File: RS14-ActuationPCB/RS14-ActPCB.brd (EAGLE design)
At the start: 105.1 x 80 mm, 34 parts, among them IC1 L293D, IC2 L293D, P12V 22-23-2021, T1 2N3904, T2 2N3904, T3 2N3904, T4 2N3904

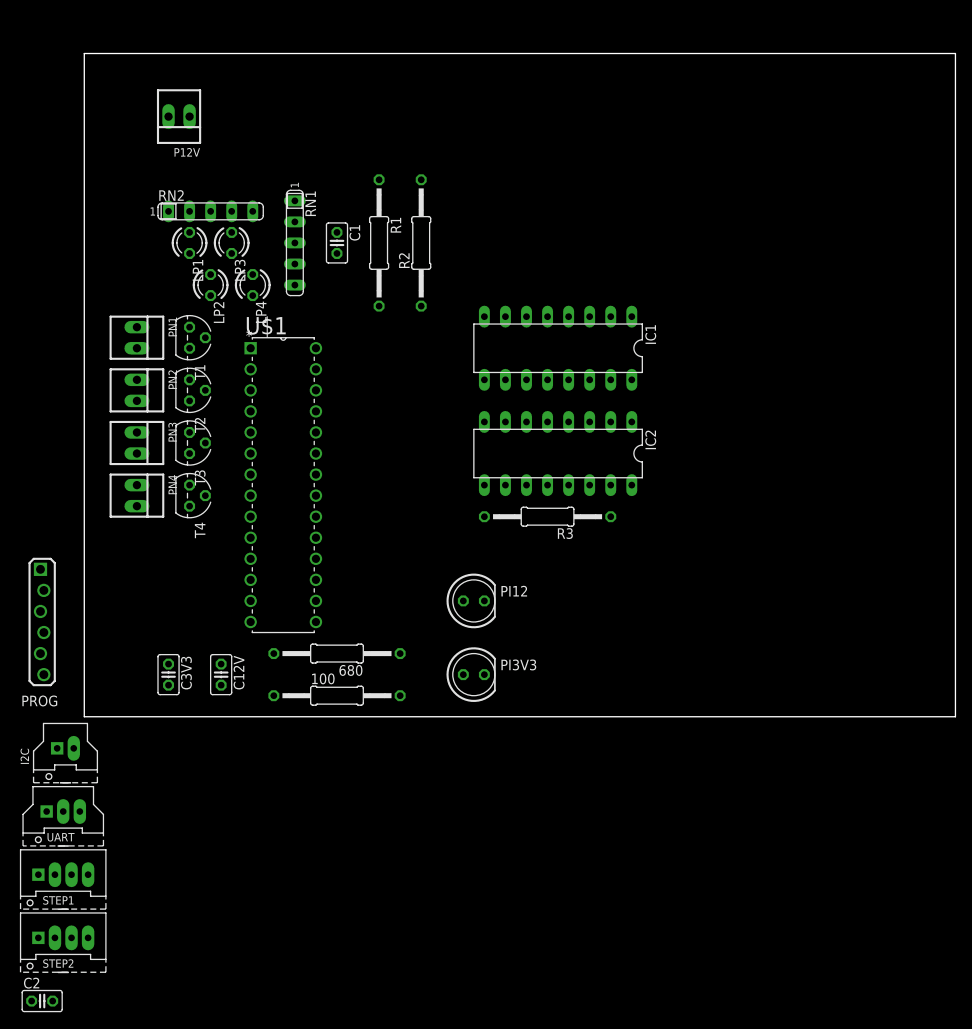
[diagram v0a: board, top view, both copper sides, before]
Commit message: Updated Actuation PCB
This is the first draft layout.

It only has two of the four desired screw holes, but this is mainly due
to my refusal to make the board bigger in my tired stubbornness. There
is also no labeling on the board (other than small built in markers) as
of yet. So this will need to be added as well.
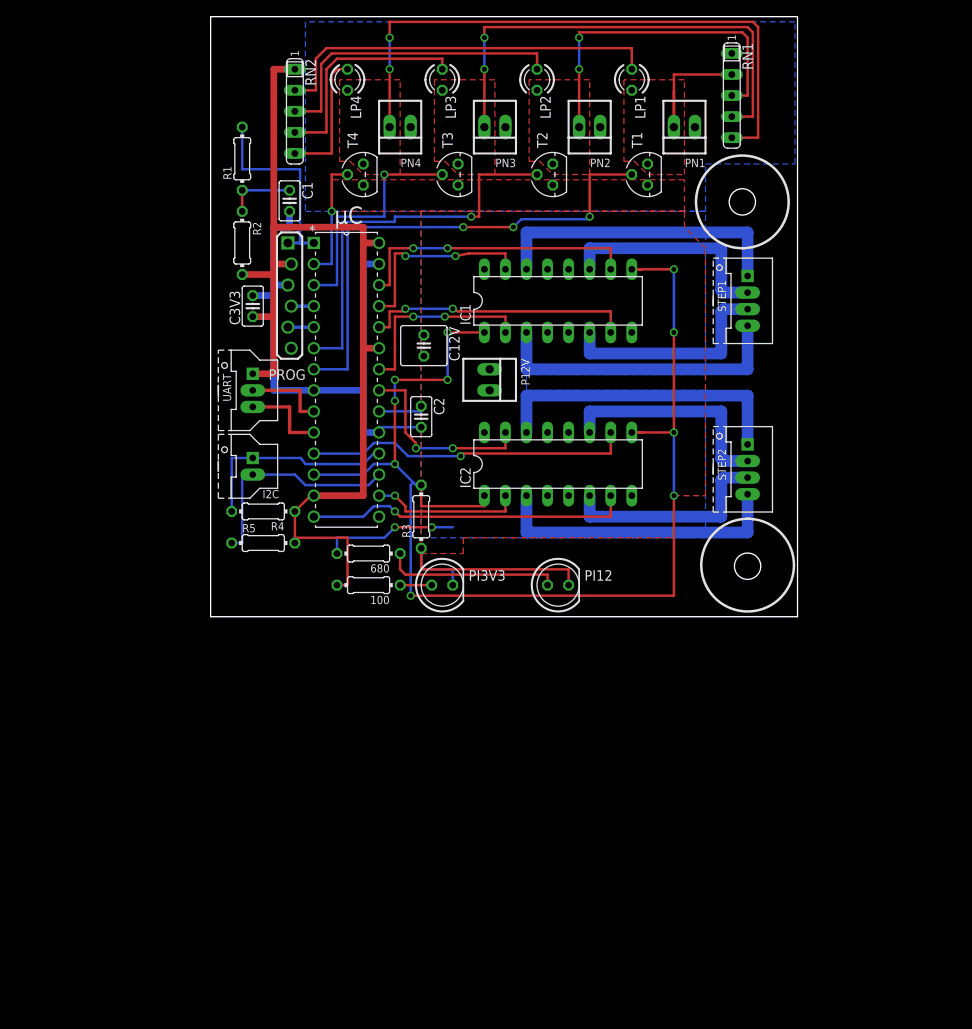
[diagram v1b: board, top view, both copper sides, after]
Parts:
- removed U$1: PIC32MX250F128B-I/SP, Microchip_By_element14_Batch_1:DIP254P762X508-28
- added R4, R5: 2K2, rcl:0204/7
- added µC: PIC32MX250F128B-I/SP, Microchip_By_element14_Batch_1:DIP254P762X508-28
- 100, 680, R1, R2, R3: device rcl:0207/15 -> rcl:0204/7
- C12V: device rcl:C025-025X050 -> rcl:C025-060X050
- moved STEP1 107.7 mm to (74.9, 50.2), turned to 270 degrees
- moved STEP2 100.0 mm to (74.9, 29.8), turned to 270 degrees
- moved C2 84.0 mm to (35.6, 36.2), turned to 270 degrees
- moved PN1 70.8 mm to (67.3, 71.1), turned to 180 degrees
- moved PN2 63.2 mm to (55.9, 71.1), turned to 180 degrees
- moved T1 58.6 mm to (62.9, 65.4), turned to 90 degrees
- moved PN3 57.6 mm to (44.5, 71.1), turned to 180 degrees
- moved LP1 56.9 mm to (61.0, 76.8)
- moved UART 55.7 mm to (15.2, 39.4), turned to 270 degrees
- moved RN1 55.6 mm to (73.0, 74.9)
- moved PN4 54.6 mm to (33.0, 71.1), turned to 180 degrees
- moved T2 51.0 mm to (51.4, 65.4), turned to 90 degrees
- moved PROG 49.4 mm to (19.7, 50.8)
- moved P12V 49.1 mm to (43.8, 40.6), turned to 270 degrees
- moved C12V 46.6 mm to (35.9, 44.8)
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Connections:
- removed net N$1: C2.2
- net 3V3: now also R4.2, R5.2, µC.13, µC.23, µC.28; no longer U$1.13, U$1.23, U$1.28
- net GND: now also C2.2, µC.19, µC.27, µC.8; no longer U$1.19, U$1.27, U$1.8
- net MCLR: now also µC.1; no longer U$1.1
- net N$2: now also µC.20; no longer U$1.20
- net PC1: now also µC.7; no longer U$1.2
- net PC2: now also µC.6; no longer U$1.3
- net PC3: now also µC.3; no longer U$1.11
- net PC4: now also µC.2; no longer U$1.12
- net PGC: now also µC.5; no longer U$1.5
- net PGD: now also µC.4; no longer U$1.4
- net SCL: now also R5.1, µC.17; no longer U$1.17
- net SDA: now also R4.1, µC.18; no longer U$1.18
- net STEP_EN: now also µC.12; no longer U$1.16
- net STEP_IN11: now also µC.22; no longer U$1.26
- net STEP_IN12: now also µC.24; no longer U$1.25
- net STEP_IN13: now also µC.26; no longer U$1.24
- net STEP_IN14: now also µC.25; no longer U$1.22
- net STEP_IN21: now also µC.16; no longer U$1.21
- net STEP_IN22: now also µC.14; no longer U$1.6
- net STEP_IN23: now also µC.11; no longer U$1.7
- net STEP_IN24: now also µC.21; no longer U$1.14
- net U1RX: now also µC.9; no longer U$1.9
- net U1TX: now also µC.10; no longer U$1.10
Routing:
- net STEP_EN: track 0.00 -> 150.2 mm, vias 0 -> 10
- net 3V3: track 0.00 -> 124.1 mm
- net GND: track 0.00 -> 98.9 mm
- net PN4: track 0.00 -> 73.9 mm, vias 0 -> 2
- net PC1: track 0.00 -> 61.3 mm, vias 0 -> 3
- net PN3: track 0.00 -> 57.4 mm, vias 0 -> 2
- net PC2: track 0.00 -> 47.9 mm, vias 0 -> 1
- net N$4: track 0.00 -> 47.5 mm
- net PN2: track 0.00 -> 40.9 mm, vias 0 -> 2
- net STEP_IN23: track 0.00 -> 39.7 mm, vias 0 -> 1
- net STEP_IN22: track 0.00 -> 39.4 mm, vias 0 -> 1
- net N$8: track 0.00 -> 37.4 mm
- net OUT_21: track 0.00 -> 37.0 mm
- net OUT_14: track 0.00 -> 36.4 mm
- net OUT_11: track 0.00 -> 36.4 mm
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- added copper zone on layer 16, net 12V
- added copper zone on layer 1, net GND
- added copper zone on layer 1, net PN1
- added copper zone on layer 1, net PN2
- added copper zone on layer 1, net PN3
- added copper zone on layer 1, net PN4
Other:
- board size 105.1 x 80 mm -> 70.8 x 72.4 mm

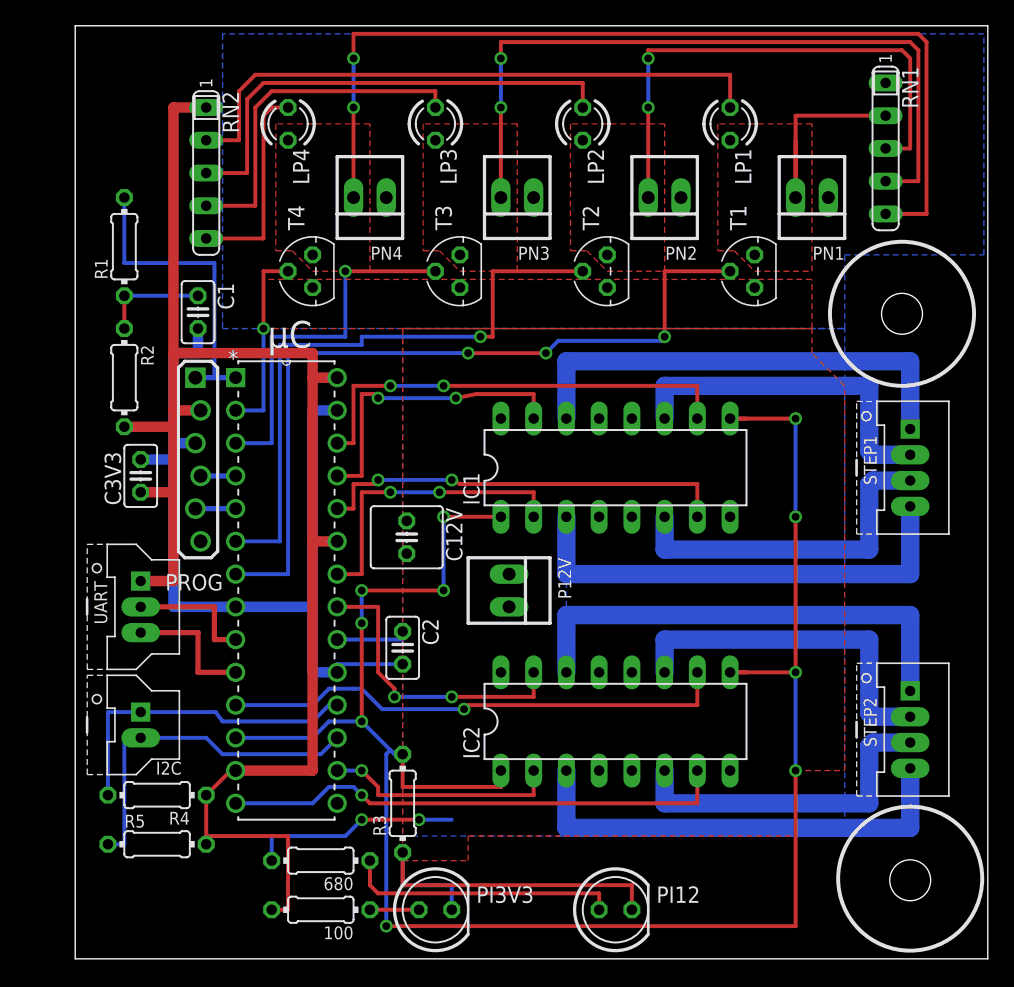
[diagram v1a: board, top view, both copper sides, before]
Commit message: Updated ActPCB with mounting holes and labels
This includes larger print labels next to each pneumatic to identify which number of the pneumatic is being used, as well as large pring STEP1 and STEP2 next to each header to make them more visible.
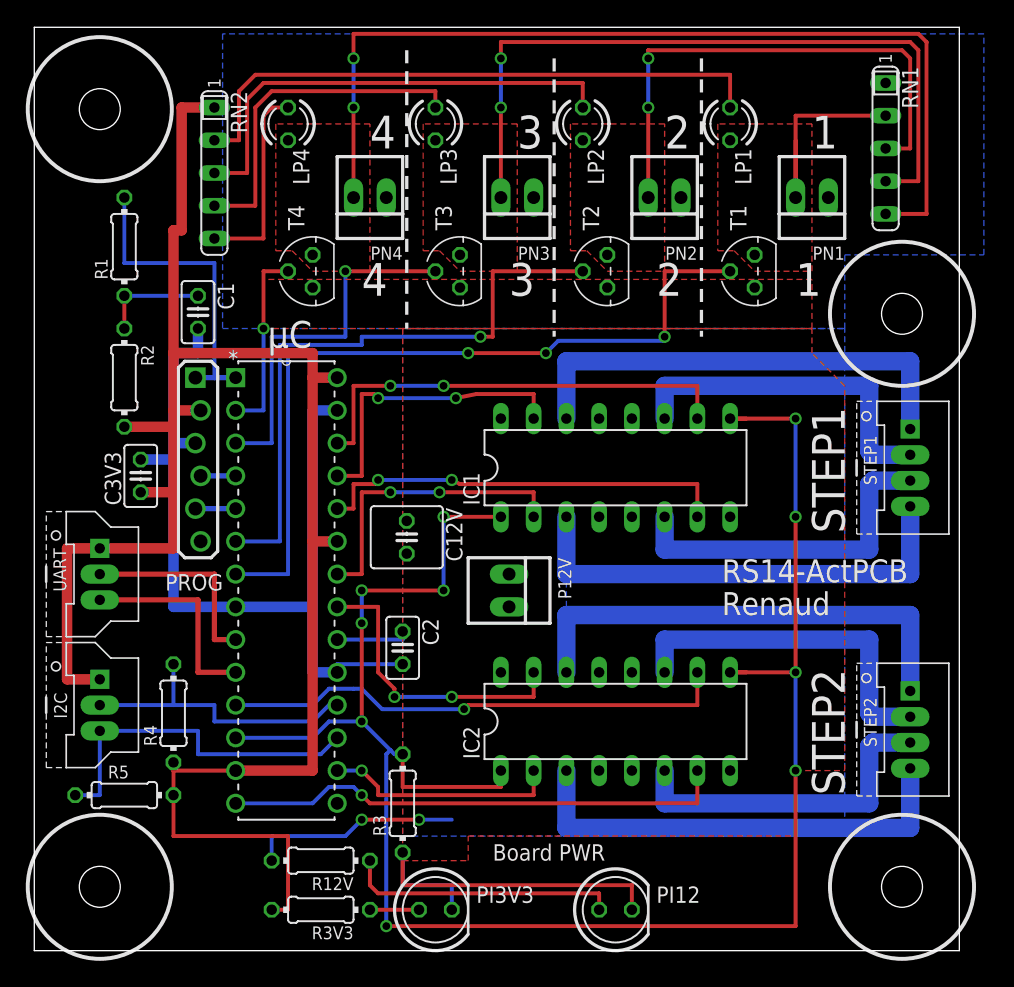
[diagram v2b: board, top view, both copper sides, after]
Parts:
- I2C: value SHERLOCK-2PVERTICAL -> SHERLOCK-3PVERTICAL; device rs-molex-sherlock:35362-02** -> rs-molex-sherlock:35362-03**
- R12V: value (none) -> 680
- R3V3: value (none) -> 100
- moved R4 6.48 mm to (17.8, 31.1), turned to 270 degrees
- moved R5 4.58 mm to (14.0, 24.8)
- moved I2C 4.07 mm to (12.1, 31.8)
- moved UART 4.07 mm to (12.1, 41.9)
- moved RN2 0.63 mm to (21.0, 73.0)
- renumbered 100 to R3V3, 680 to R12V
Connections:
- net 3V3: now also I2C.P1
- net SCL: now also I2C.P3; no longer I2C.P2
- net SDA: now also I2C.P2; no longer I2C.P1
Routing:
- net 3V3: track 124.1 -> 146.2 mm
- net U1TX: track 10.4 -> 16.2 mm
- net U1RX: track 9.91 -> 15.6 mm
- net SDA: track 25.1 -> 23.4 mm
- net N$9: track 27.2 -> 26.6 mm
- net N$8: track 37.4 -> 36.7 mm
- net N$4: track 47.5 -> 46.9 mm
- net N$10: track 16.1 -> 15.5 mm
- net SCL: track 27.1 -> 27.6 mm
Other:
- board size 70.8 x 72.4 mm -> 71.8 x 71.6 mm
- board text added: "1"
- board text added: "12V Pneumatic Drivers"
- board text added: "2"
- board text added: "3"
- board text added: "4"
- board text added: "Board PWR"
- board text added: "Dual Stepper Motor Controllers"
- board text added: "RS14-ActPCB"
- board text added: "Renaud"
- board text added: "STEP1"
- board text added: "STEP2"

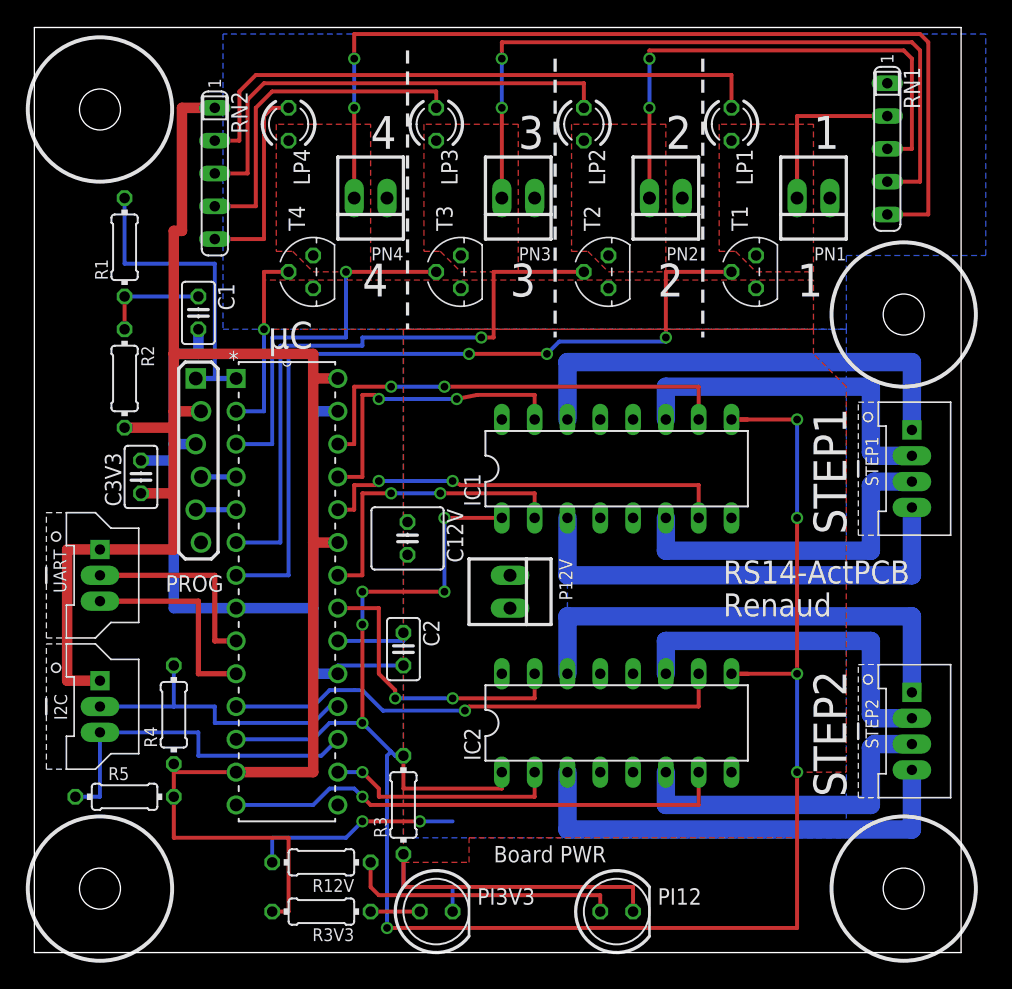
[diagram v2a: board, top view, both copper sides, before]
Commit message: Quick DRC fix with board area.
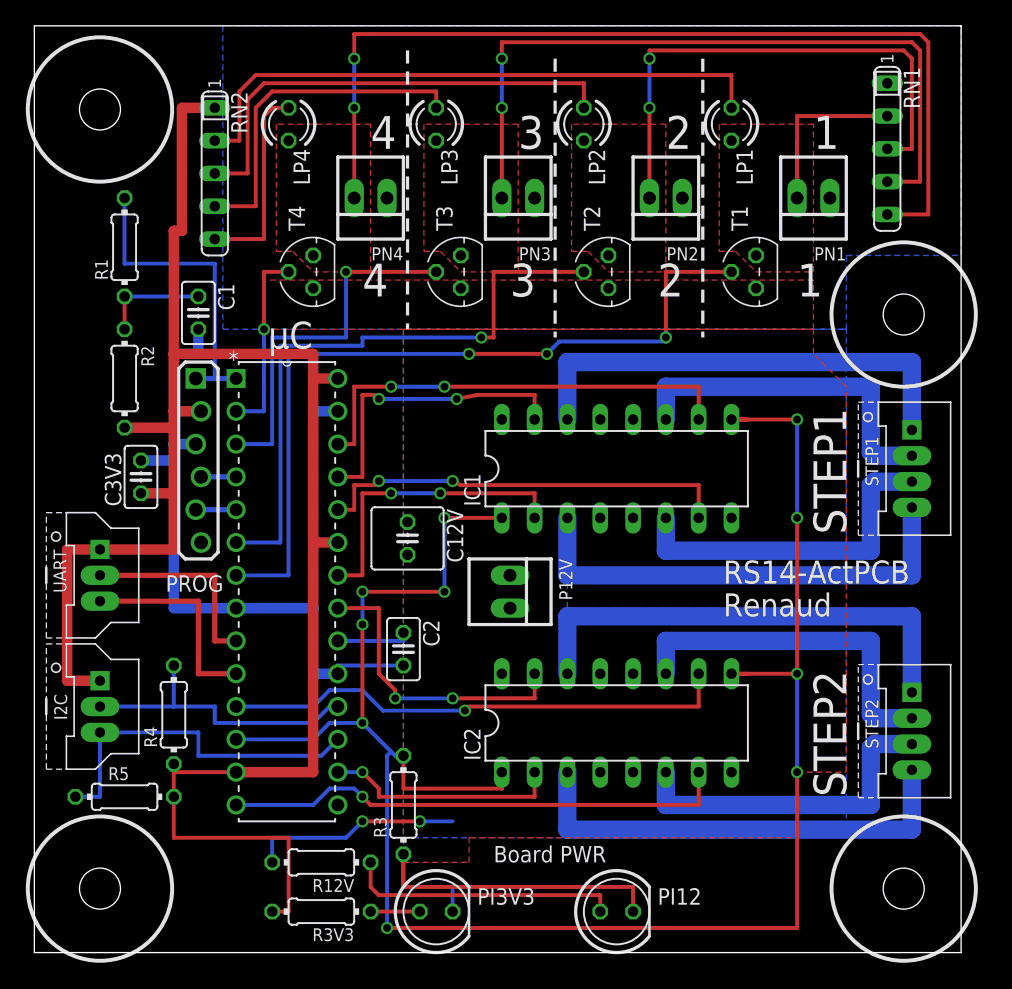
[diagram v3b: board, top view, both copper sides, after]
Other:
- board size 71.8 x 71.6 mm -> 71.8 x 71.8 mm
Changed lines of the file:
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@@
 <plain>
 <wire x1="6.985" y1="12.7" x2="78.74" y2="12.7" width="0" layer="20"/>
-<wire x1="78.74" y1="12.7" x2="78.74" y2="84.328" width="0" layer="20"/>
-<wire x1="78.74" y1="84.328" x2="6.985" y2="84.328" width="0" layer="20"/>
-<wire x1="6.985" y1="84.328" x2="6.985" y2="12.7" width="0" layer="20"/>
+<wire x1="78.74" y1="12.7" x2="78.74" y2="84.455" width="0" layer="20"/>
+<wire x1="78.74" y1="84.455" x2="6.985" y2="84.455" width="0" layer="20"/>
+<wire x1="6.985" y1="84.455" x2="6.985" y2="12.7" width="0" layer="20"/>
 <circle x="74.295" y="17.653" radius="5.588" width="0.3048" layer="21"/>
 <circle x="74.295" y="62.103" radius="5.588" width="0.3048" layer="21"/>
@@
 <vertex x="69.85" y="60.96"/>
 <vertex x="69.85" y="66.675"/>
-<vertex x="80.645" y="66.675"/>
-<vertex x="80.645" y="83.82"/>
-<vertex x="21.59" y="83.82"/>
+<vertex x="78.74" y="66.675"/>
+<vertex x="78.74" y="84.455"/>
+<vertex x="21.59" y="84.455"/>
 </polygon>
 <polygon width="0.3048" layer="16">
